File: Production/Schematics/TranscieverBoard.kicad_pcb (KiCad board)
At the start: 2 copper layers, 6 parts, among them J1 1909763-1, J2 Conn_01x10_Male, J3 Conn_01x10_Male, J4 Conn_01x10_Male, J5 Conn_01x10_Male, U1 MAX7037EGL+

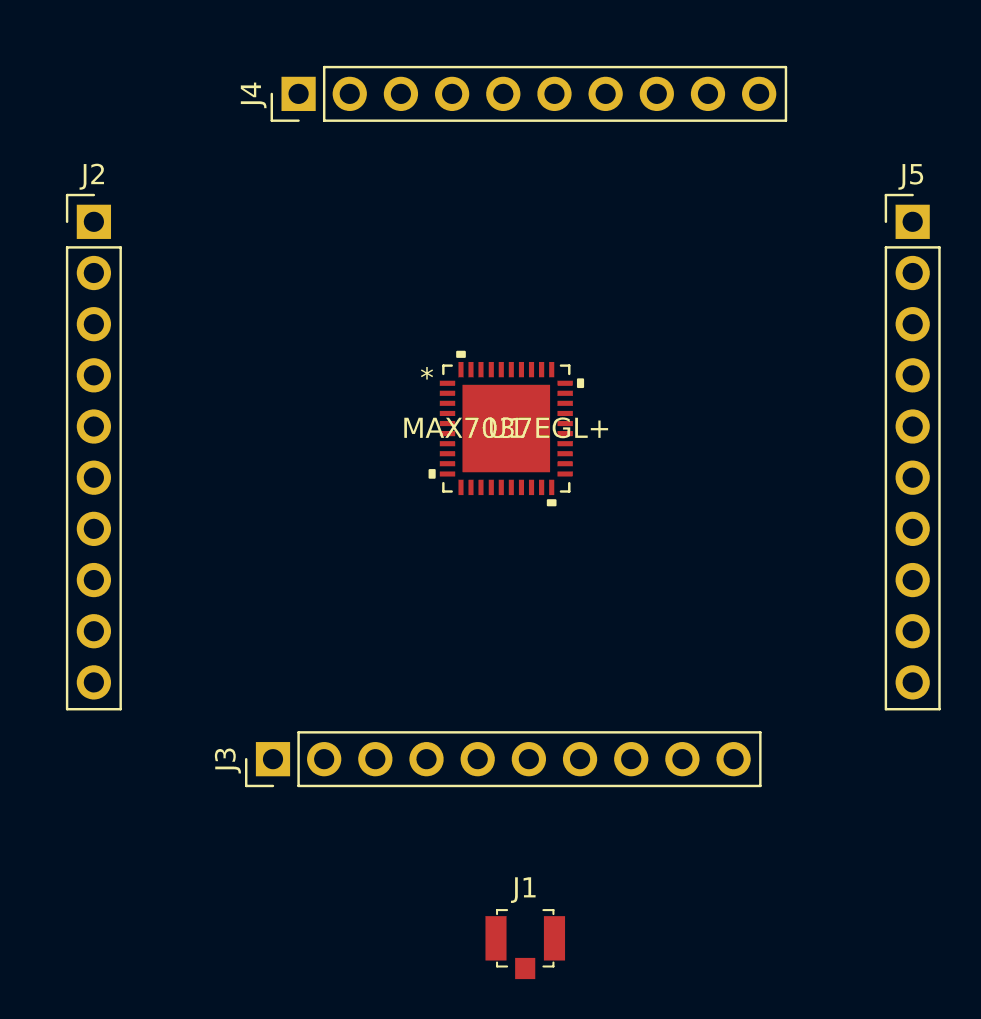
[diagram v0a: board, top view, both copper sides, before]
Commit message: Gerber Files Generated
Gerber Files for transceiver module PCB generated
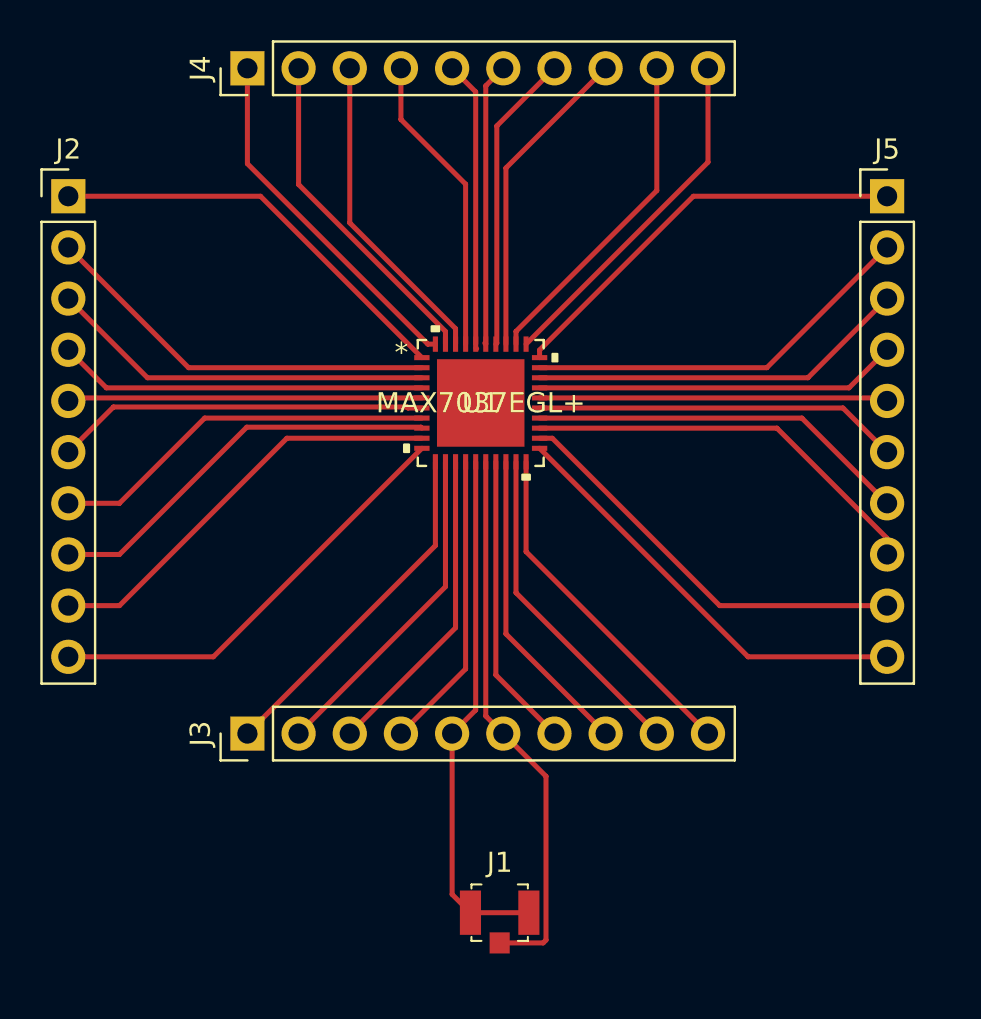
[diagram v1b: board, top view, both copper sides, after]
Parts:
- moved J4 2.84 mm to (104.1, 55.9)
- moved J5 1.80 mm to (135.9, 62.2)
- moved J1 1.80 mm to (116.7, 97.8)
- moved J2 1.80 mm to (95.2, 62.2)
- moved J3 1.80 mm to (104.1, 88.9)
- moved U1 1.80 mm to (115.7, 72.5)
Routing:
- net Net-(J1-Pad2): track 0.00 -> 27.3 mm
- net Net-(J1-Pad1): track 0.00 -> 26.1 mm
- net Net-(J2-Pad10): track 0.00 -> 21.8 mm
- net Net-(J5-Pad10): track 0.00 -> 21.5 mm
- net Net-(J2-Pad9): track 0.00 -> 21.0 mm
- net Net-(J2-Pad1): track 0.00 -> 20.9 mm
- net Net-(J5-Pad1): track 0.00 -> 20.8 mm
- net Net-(J5-Pad9): track 0.00 -> 20.7 mm
- net Net-(J5-Pad8): track 0.00 -> 20.3 mm
- net Net-(J2-Pad8): track 0.00 -> 20.2 mm
- net Net-(J2-Pad2): track 0.00 -> 20.0 mm
- net Net-(J5-Pad2): track 0.00 -> 19.7 mm
- net Net-(J2-Pad7): track 0.00 -> 19.3 mm
- net Net-(J2-Pad3): track 0.00 -> 19.2 mm
- net Net-(J5-Pad7): track 0.00 -> 19.0 mm
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
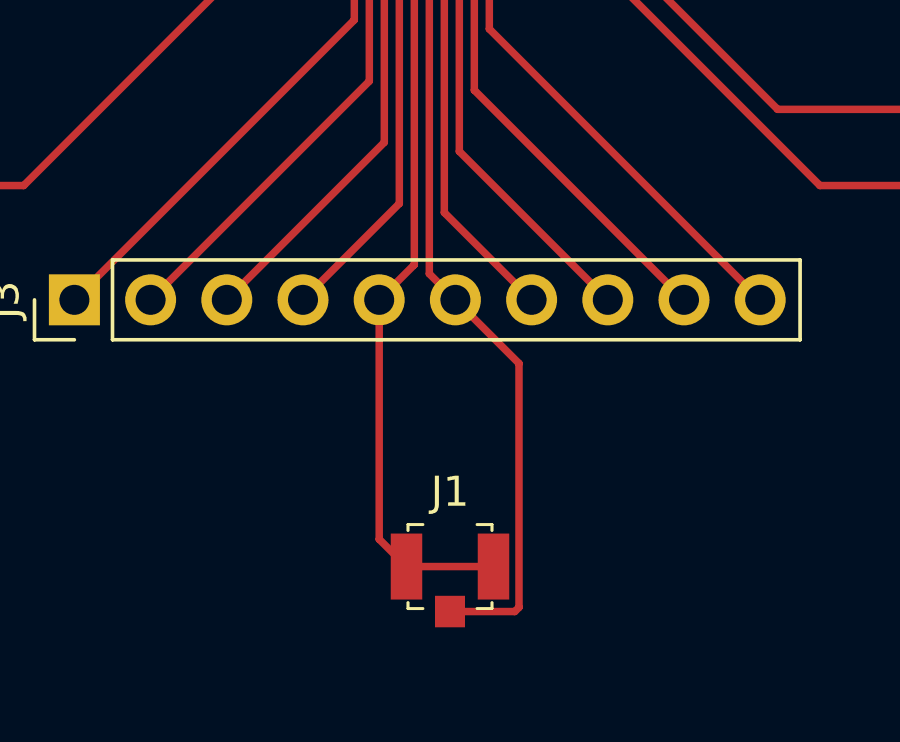
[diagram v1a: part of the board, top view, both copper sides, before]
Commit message: Updated PCB
Updated PCB from MCX to SMA
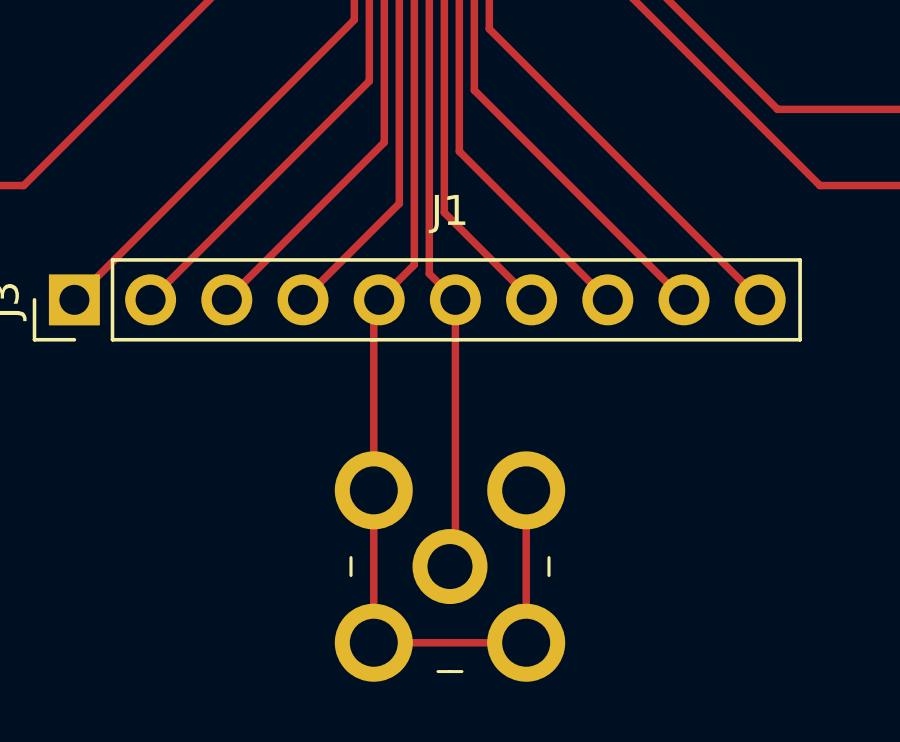
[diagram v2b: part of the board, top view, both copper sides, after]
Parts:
- J1: value 1909763-1 -> 5-1814400-1; footprint digikey-footprints:UMCoax_Pin_1909763-1 -> digikey-footprints:RF_SMA_RightAngle_5-1814400-1
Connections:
- J3 pad 5: Net-(J1-Pad1) -> Net-(J1-Pad2)
- J3 pad 6: Net-(J1-Pad2) -> Net-(J1-Pad1)
- U1 pad 15: Net-(J1-Pad1) -> Net-(J1-Pad2)
- U1 pad 16: Net-(J1-Pad2) -> Net-(J1-Pad1)
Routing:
- net Net-(J1-Pad2): track 27.3 -> 35.8 mm
- net Net-(J1-Pad1): track 26.1 -> 22.8 mm

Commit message: PCB Design update
PCB schematic update
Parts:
- added C10: .1uF, Capacitor_SMD:C_0603_1608Metric, F.Cu at (128.3, 91.4)
- added C12: .1uF, Capacitor_SMD:C_0603_1608Metric, F.Cu at (120.7, 83.8)
- added C22: 220pF, Capacitor_SMD:C_0402_1005Metric, F.Cu at (128.3, 88.9)
- added C23: 220pF, Capacitor_SMD:C_0402_1005Metric, F.Cu at (120.7, 81.3)
- added C24: 220pF, Capacitor_SMD:C_0402_1005Metric, F.Cu at (128.3, 99.1)
- added C26: 820pF, Capacitor_SMD:C_0603_1608Metric, F.Cu at (114.3, 110.0)
- added C29: 220pF, Capacitor_SMD:C_0402_1005Metric, F.Cu at (127.0, 102.9)
- added C3: 1.5pF, Capacitor_SMD:C_0402_1005Metric, F.Cu at (115.1, 96.5)
- added C32: 220pF, Capacitor_SMD:C_0402_1005Metric, F.Cu at (127.0, 101.6)
- added C34: 1.8pF, Capacitor_SMD:C_0402_1005Metric, F.Cu at (106.7, 101.6)
- added C35: 1.8pF, Capacitor_SMD:C_0402_1005Metric, F.Cu at (120.7, 104.9)
- added C36: 220pF, Capacitor_SMD:C_0402_1005Metric, F.Cu at (124.5, 105.4)
- added C5: 220pF, Capacitor_SMD:C_0402_1005Metric, F.Cu at (110.0, 83.8)
- added C6: .1uF, Capacitor_SMD:C_0603_1608Metric, F.Cu at (109.7, 81.3)
- added L4: 100nH, Inductor_SMD:L_0402_1005Metric, F.Cu at (124.5, 99.1)
- added L5: 18nH, Inductor_SMD:L_0402_1005Metric, F.Cu at (109.2, 104.6)
- added L6: 18nH, Inductor_SMD:L_0402_1005Metric, F.Cu at (113.0, 99.1)
- added L7: 18nH, Inductor_SMD:L_0402_1005Metric, F.Cu at (116.8, 99.1)
- added L8: 18nH, Inductor_SMD:L_0402_1005Metric, F.Cu at (123.2, 101.6)
- added L9: 18nH, Inductor_SMD:L_0402_1005Metric, F.Cu at (115.1, 91.4)
- added R22: 0, Resistor_SMD:R_0402_1005Metric, F.Cu at (119.4, 108.0)
- added R23: 0, Resistor_SMD:R_0402_1005Metric, F.Cu at (110.5, 108.0)
- added R31: 0, Resistor_SMD:R_0402_1005Metric, F.Cu at (110.5, 101.6)
- added R32: 0, Resistor_SMD:R_0402_1005Metric, F.Cu at (119.4, 101.6)
- added U2: C3E-16.000-8-2050-X1-CT, ul_C3E-16-000-8-2050-X1-CT:C3E-16.000-8-2050-X1-CT, F.Cu at (167.5, 44.7)
- J1: value 5-1814400-1 -> 5-1814832-1; footprint digikey-footprints:RF_SMA_RightAngle_5-1814400-1 -> digikey-footprints:RF_SMA_Vertical_5-1814832-1
- J3: value Conn_01x10_Male -> Conn_01x02; footprint Connector_PinHeader_2.54mm:PinHeader_1x10_P2.54mm_Vertical -> Connector_PinHeader_2.54mm:PinHeader_1x02_P2.54mm_Vertical
- moved J1 21.7 mm to (114.3, 119.4)
- moved J3 21.3 mm to (124.5, 95.2)
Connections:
- J1 pad 2: Net-(J1-Pad2) -> Net-(C26-Pad2)
- J3 pad 1: Net-(J3-Pad1) -> Net-(C24-Pad1)
- J3 pad 2: Net-(J3-Pad2) -> Net-(C10-Pad1)
- U1 pad 11: Net-(J3-Pad1) -> Net-(C5-Pad2)
- U1 pad 12: Net-(J3-Pad2) -> Net-(U1-Pad12)
- U1 pad 13: Net-(J3-Pad3) -> TEST2
- U1 pad 14: Net-(J3-Pad4) -> GND
- U1 pad 15: Net-(J1-Pad2) -> Net-(C3-Pad1)
- U1 pad 16: Net-(J1-Pad1) -> Net-(C3-Pad2)
- U1 pad 17: Net-(J3-Pad7) -> GND
- U1 pad 18: Net-(J3-Pad8) -> Net-(C10-Pad1)
- U1 pad 19: Net-(J3-Pad9) -> Net-(C12-Pad1)
- U1 pad 20: Net-(J3-Pad10) -> TEST1
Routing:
- net Net-(J1-Pad2): track 35.8 -> 0.00 mm
- net Net-(C10-Pad1): track 0.00 -> 31.7 mm
- net Net-(C3-Pad1): track 0.00 -> 24.2 mm
- net Net-(C3-Pad2): track 0.00 -> 23.9 mm
- net Net-(J1-Pad1): track 22.8 -> 0.00 mm
- net GND: track 0.00 -> 20.9 mm
- net Net-(J3-Pad1): track 17.4 -> 0.00 mm
- net Net-(J3-Pad10): track 17.2 -> 0.00 mm
- net Net-(J3-Pad2): track 16.5 -> 0.00 mm
- net Net-(J3-Pad9): track 16.4 -> 0.00 mm
- net Net-(J3-Pad3): track 15.7 -> 0.00 mm
- net Net-(J3-Pad8): track 15.5 -> 0.00 mm
- net Net-(J3-Pad4): track 14.8 -> 0.00 mm
- net Net-(J3-Pad7): track 14.7 -> 0.00 mm
- net Net-(C5-Pad2): track 0.00 -> 13.3 mm
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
